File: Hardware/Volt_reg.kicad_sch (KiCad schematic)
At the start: 45 parts, among them Q2 BSZ025N04LS, Q3 BSZ025N04LS, Q4 BUK9M11-40EX, Q5 BUK9M11-40EX, U10 TPS55288QRPMRQ1, U8 INA219AxDCN, U9 LM74810

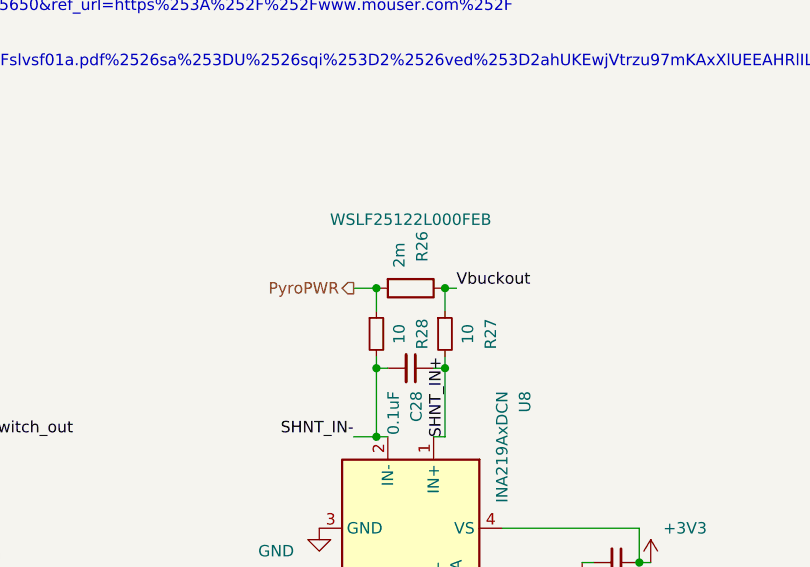
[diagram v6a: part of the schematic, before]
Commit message: Swapped battery & nichrome positions
fixed crystal and other small things
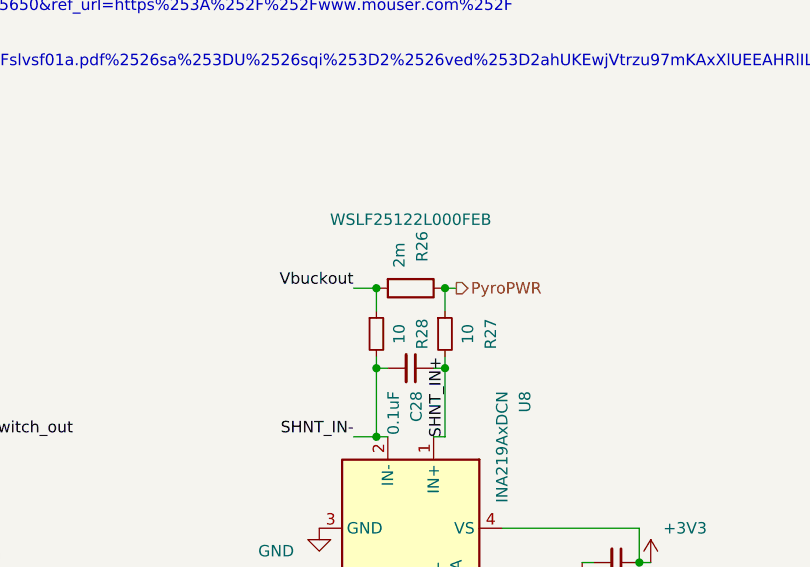
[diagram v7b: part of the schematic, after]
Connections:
- net ISN_2: now also R26.2, R28.1; no longer R26.1, R27.1
- net PyroPWR: now also R26.1, R27.1; no longer R26.2, R28.1
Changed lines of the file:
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@@
+		)
+	)
+	(label "Vbuckout"
+		(at 201.93 55.88 180)
+		(effects
+			(font
+				(size 1.27 1.27)
+			)
+			(justify right bottom)
 		)
 	)
@@
 	(label "DR1L_2"
 		(at 118.11 182.88 0)
-		(effects
-			(font
-				(size 1.27 1.27)
-			)
-			(justify left bottom)
-		)
-	)
-	(label "Vbuckout"
-		(at 213.36 55.88 0)
 		(effects
 			(font
@@
 		)
 	)
+	(hierarchical_label "PyroPWR"
+		(shape output)
+		(at 213.36 55.88 0)
+		(effects
+			(font
+				(size 1.27 1.27)
+			)
+			(justify left)
+		)
+	)
 	(hierarchical_label "SDA-BuckBC"
 		(shape bidirectional)
@@
 		(effects
 			(font
-				(size 1.27 1.27)
-			)
-			(justify right)
-		)
-	)
-	(hierarchical_label "PyroPWR"
-		(shape output)
-		(at 201.93 55.88 180)
-		(effects
-			(font

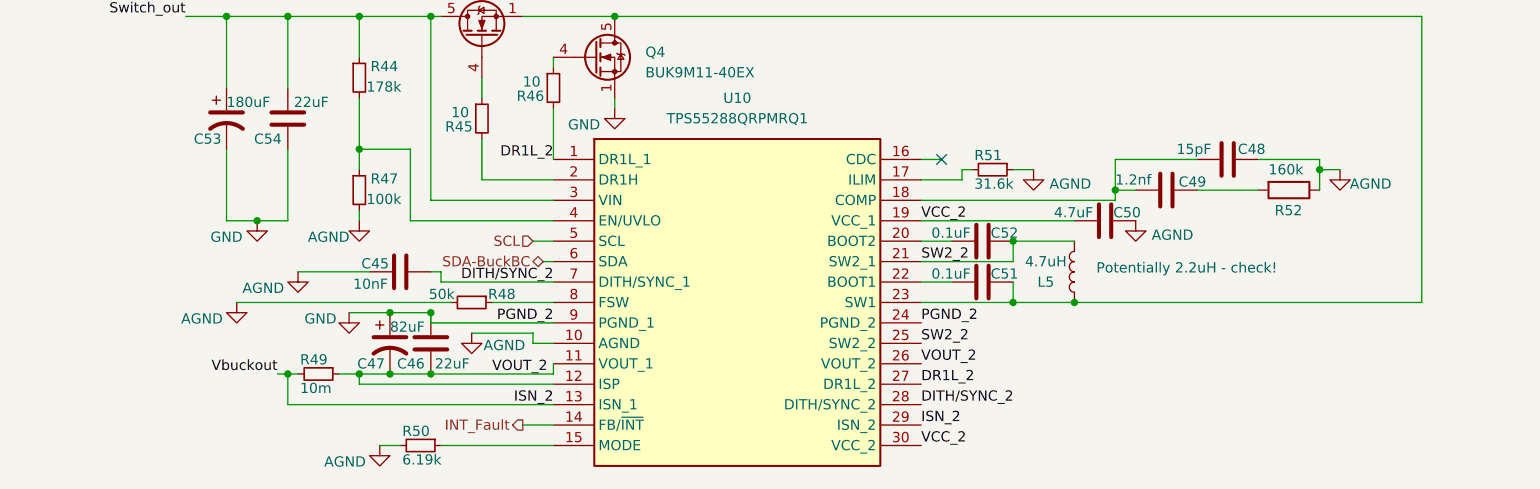
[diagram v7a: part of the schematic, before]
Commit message: Testpoints + footprints + AGND plane
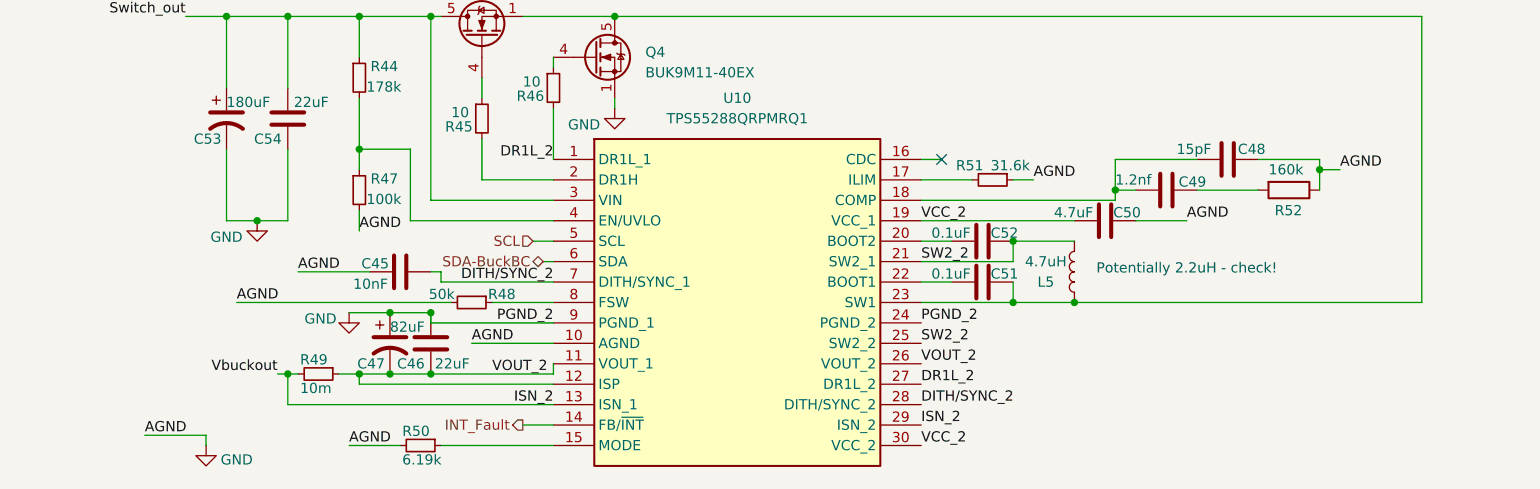
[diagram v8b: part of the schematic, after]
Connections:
- net AGND is gone; now on net GND: C45.2, C48.1, C50.1, R47.2, R48.2, R50.2, R51.1, R52.1, U10.10 (AGND)
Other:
- moved on the sheet: R51
